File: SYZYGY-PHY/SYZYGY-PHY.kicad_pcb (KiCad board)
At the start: 4 copper layers, 57.7 x 27 mm, 48 parts, among them J1 QTH-020-01-X-D-DP-A, J2 ARJM11C7-502-KB-EW2, J3 Conn_01x10, U1 GPY111, U2 TXB0106RGY, U3 TXB0106RGY, Y1 Crystal_GND24

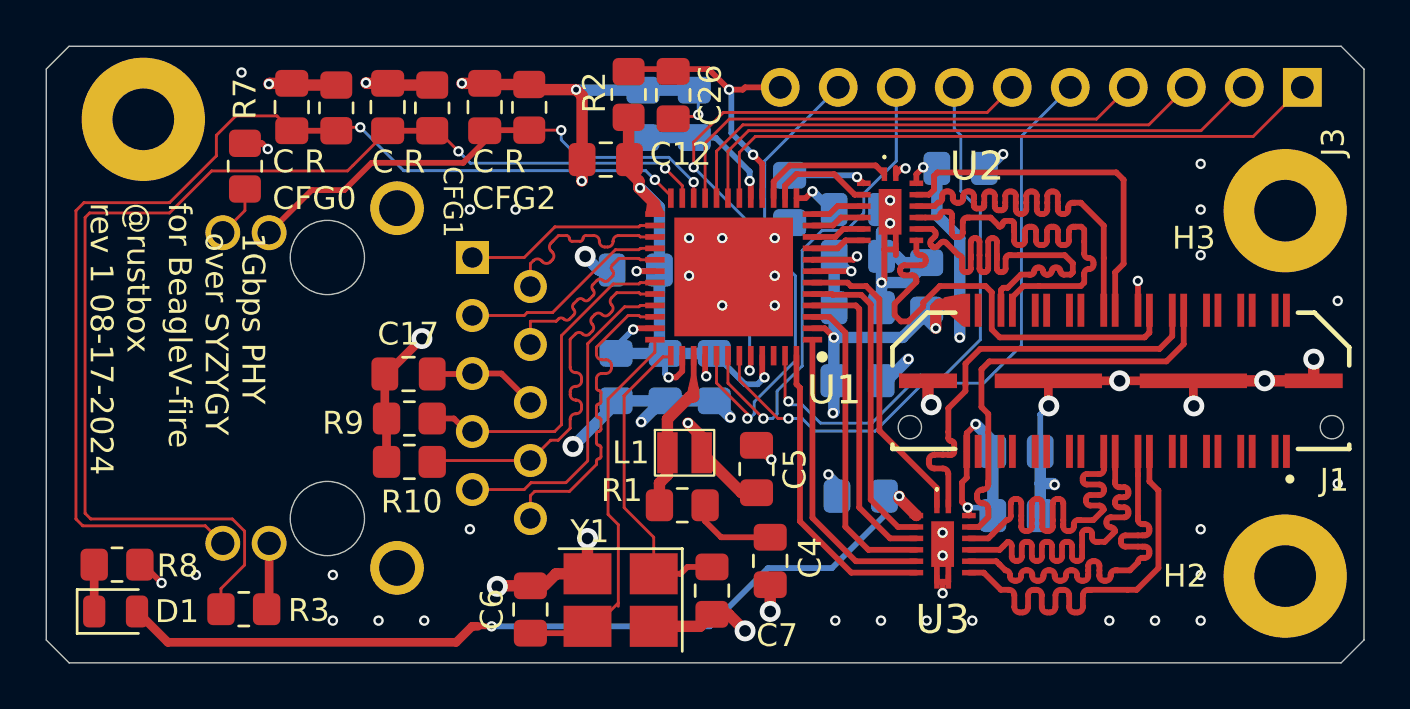
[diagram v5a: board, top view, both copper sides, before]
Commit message: adding a GND header, adding 3.3V and 1.8V 1x2 header
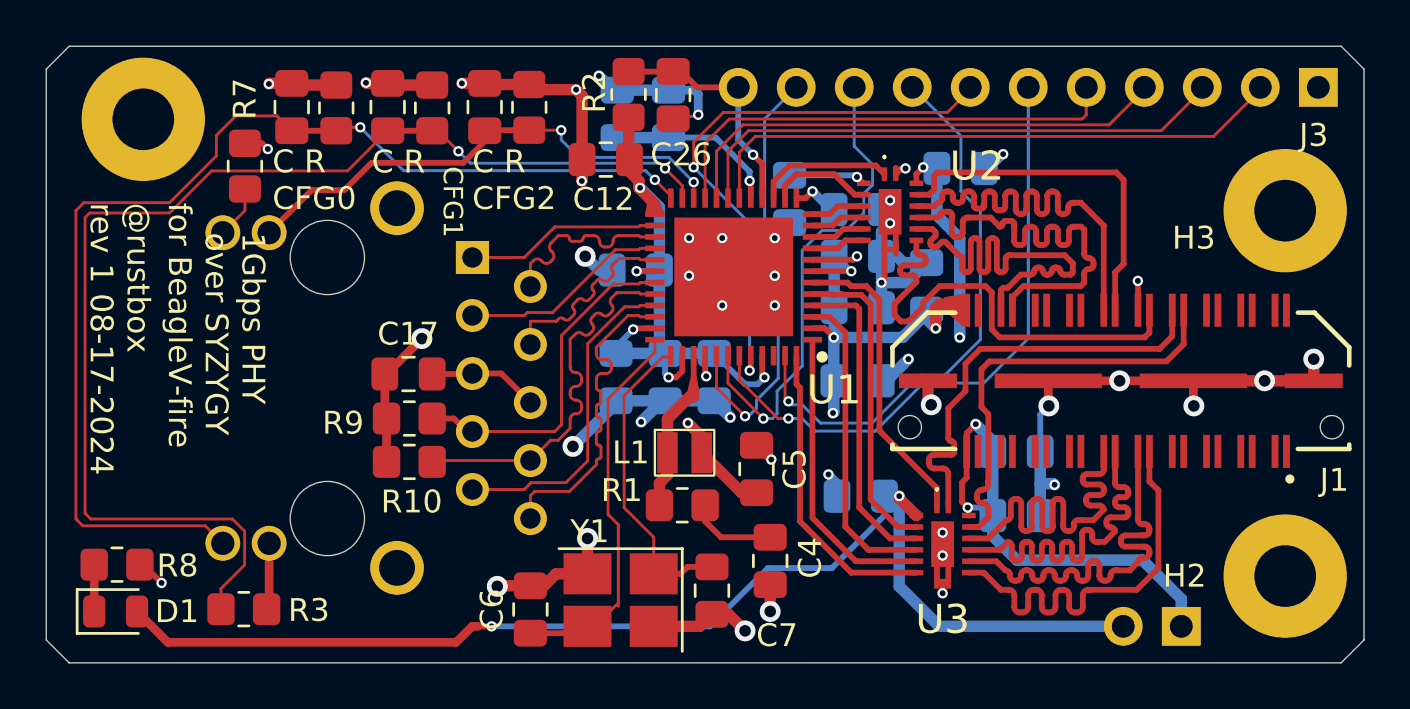
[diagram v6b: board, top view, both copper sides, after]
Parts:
- added J4: Conn_01x02, Connector_PinHeader_2.54mm:PinHeader_1x02_P2.54mm_Vertical, B.Cu at (139.7, 87.4)
- J3: value Conn_01x10 -> Conn_01x11; footprint Connector_PinSocket_2.54mm:PinSocket_1x10_P2.54mm_Vertical -> Connector_PinSocket_2.54mm:PinSocket_1x11_P2.54mm_Vertical
- moved C16 1.12 mm to (115.0, 65.0)
- moved C18 1.12 mm to (117.2, 65.0)
- moved J3 0.70 mm to (145.7, 63.8)
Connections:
- J3 pad 1: /TDI -> GND
- J3 pad 10: /RSTN -> /MDC
- J3 pad 2: /TCK -> /TDI
- J3 pad 3: /TMS -> /TCK
- J3 pad 4: /TDO -> /TMS
- J3 pad 5: /SCL -> /TDO
- J3 pad 6: /SDA -> /SCL
- J3 pad 7: /MDINT -> /SDA
- J3 pad 8: /MDIO -> /MDINT
- J3 pad 9: /MDC -> /MDIO
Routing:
- net +3V3: track 102.4 -> 116.2 mm
- net +1V8: track 23.3 -> 34.8 mm
- net GND: track 98.3 -> 107.6 mm, vias 64 -> 42
- net /RSTN: track 12.4 -> 10.4 mm, vias 2 -> 1
- net /MDC: track 20.6 -> 19.1 mm
- net /SDA: track 26.6 -> 25.2 mm
- net /TCK: track 25.8 -> 24.4 mm
- net /TMS: track 23.8 -> 22.3 mm
- net /TDI: track 27.8 -> 26.4 mm
- net /TDO: track 21.9 -> 20.8 mm
- net /VDDLC: track 35.1 -> 36.2 mm
- net /SCL: track 28.1 -> 27.3 mm
- net /MDINT: track 23.9 -> 24.7 mm
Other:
- board text added: "+1V8"
- board text added: "+3V3"
- board text added: "GND"

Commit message: make DRC happier with a "solid" connection
Instead of "thermal relief" where there isn't really room for it,
connect to the zones by just allowing the fill to pour over the whole
area.
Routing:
- net GND: track 107.6 -> 96.6 mm
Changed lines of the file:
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@@
 		(tags "mounting hole 2.7mm m2.5")
 		(property "Reference" "H1"
-			(at 3.85 -1.05 -0)
+			(at 3.85 -1.05 0)
 			(layer "B.SilkS")
 			(effects
@@
 		(tags "resistor handsolder")
 		(property "Reference" "R3"
-			(at 2.85 0.05 360)
+			(at 2.85 0.05 0)
 			(layer "F.SilkS")
 			(effects
@@
 		)
 		(property "Value" "RLED"
-			(at 0 1.65 360)
+			(at 0 1.65 0)
 			(layer "F.Fab")
 			(effects
@@
 		)
 		(fp_text user "${REFERENCE}"
-			(at 0 0 360)
+			(at 0 0 0)
 			(layer "F.Fab")
 			(effects
@@
 		)
 		(fp_text user "${REFERENCE}"
-			(at 0 -1.27 360)
+			(at 0 -1.27 0)
 			(layer "B.Fab")
 			(effects
@@
 		(tags "Through hole socket strip THT 1x11 2.54mm single row")
 		(property "Reference" "J3"
-			(at -2.1 -0.2 -180)
+			(at -2.1 -0.2 180)
 			(layer "F.SilkS")
 			(effects
@@
 		)
 		(fp_text user "${REFERENCE}"
-			(at 0 -12.7 360)
+			(at 0 -12.7 0)
 			(layer "B.Fab")
 			(effects
@@
 			(pinfunction "Pin_1")
 			(pintype "passive")
+			(zone_connect 2)
 		)
 		(pad "2" thru_hole oval
@@
 		(net 47)
 	)
-	(segment
-		(start 145.7 63.8)
-		(end 146.85 63.8)
-		(width 0.5)
-		(layer "In1.Cu")
-		(net 47)
-	)
-	(segment
-		(start 146.85 63.8)
-		(end 146.95 63.9)
-		(width 0.5)
-		(layer "In1.Cu")
-		(net 47)
-	)
-	(segment
-		(start 146.95 64)
-		(end 146.95 65.5)
-		(width 0.5)
-		(layer "In1.Cu")
-		(net 47)
-	)
-	(segment
-		(start 144.4 64.1)
-		(end 144.4 65.3)
-		(width 0.5)
-		(layer "In1.Cu")
-		(net 47)
-	)
-	(segment
-		(start 145.7 63.8)
-		(end 144.7 63.8)
-		(width 0.5)
-		(layer "In1.Cu")
-		(net 47)
-	)
-	(segment
-		(start 144.5 64)
-		(end 144.4 64.1)
-		(width 0.5)
-		(layer "In1.Cu")
-		(net 47)
-	)
-	(segment
-		(start 144.7 63.8)
-		(end 144.5 64)
-		(width 0.5)
-		(layer "In1.Cu")
-		(net 47)
-	)
-	(segment
-		(start 146.95 63.9)
-		(end 146.95 64)
-		(width 0.5)
-		(layer "In1.Cu")
-		(net 47)
-	)
-	(segment
-		(start 144.7 63.8)
-		(end 144.5 64)
-		(width 0.5)
-		(layer "In2.Cu")
-		(net 47)
-	)
-	(segment
-		(start 146.95 64)
-		(end 146.95 65.5)
-		(width 0.5)
-		(layer "In2.Cu")
-		(net 47)
-	)
-	(segment
-		(start 145.7 63.8)
-		(end 146.85 63.8)
-		(width 0.5)
-		(layer "In2.Cu")
-		(net 47)
-	)
-	(segment
-		(start 144.5 64)
-		(end 144.4 64.1)
-		(width 0.5)
-		(layer "In2.Cu")
-		(net 47)
-	)
-	(segment
-		(start 146.85 63.8)
-		(end 146.95 63.9)
-		(width 0.5)
-		(layer "In2.Cu")
-		(net 47)
-	)
-	(segment
-		(start 144.4 64.1)
-		(end 144.4 65.3)
-		(width 0.5)
-		(layer "In2.Cu")
-		(net 47)
-	)
-	(segment
-		(start 146.95 63.9)
-		(end 146.95 64)
-		(width 0.5)
-		(layer "In2.Cu")
-		(net 47)
-	)
-	(segment
-		(start 145.7 63.8)
-		(end 144.7 63.8)
-		(width 0.5)
-		(layer "In2.Cu")
-		(net 47)
-	)

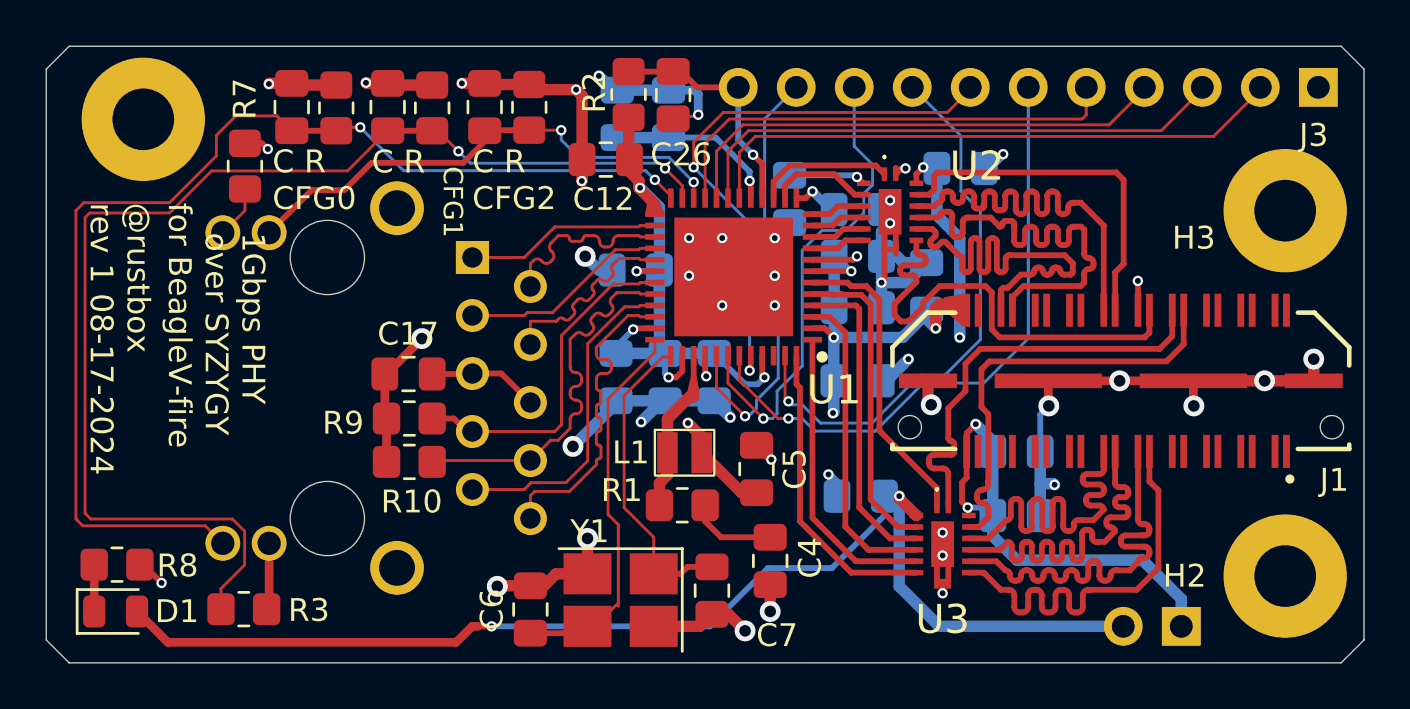
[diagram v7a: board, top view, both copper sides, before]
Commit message: adding SYZYGY breakout board, ready for review
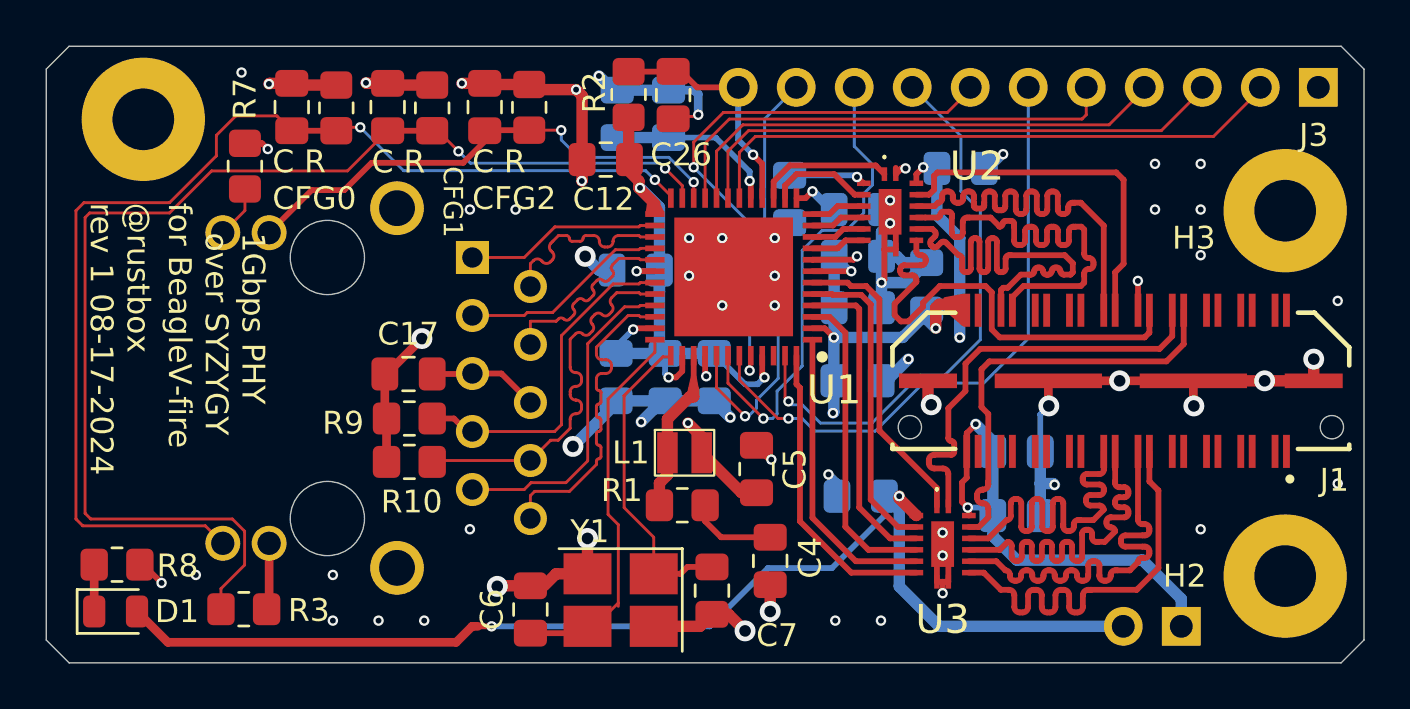
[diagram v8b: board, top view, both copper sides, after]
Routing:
- net GND: vias 42 -> 61
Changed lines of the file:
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@@
 	)
 	(via
+		(at 110.55 69.15)
+		(size 0.4572)
+		(drill 0.254)
+		(layers "F.Cu" "B.Cu")
+		(free yes)
+		(net 47)
+	)
+	(via
+		(at 140.55 71.15)
+		(size 0.4572)
+		(drill 0.254)
+		(layers "F.Cu" "B.Cu")
+		(free yes)
+		(net 47)
+	)
+	(via
 		(at 121.9 73.35)
 		(size 0.4572)
@@
 	)
 	(via
+		(at 126.55 87.15)
+		(size 0.4572)
+		(drill 0.254)
+		(layers "F.Cu" "B.Cu")
+		(free yes)
+		(net 47)
+	)
+	(via
 		(at 134.15 81.2)
 		(size 0.4572)
@@
 	)
 	(via
+		(at 146.55 73.15)
+		(size 0.4572)
+		(drill 0.254)
+		(layers "F.Cu" "B.Cu")
+		(free yes)
+		(net 47)
+	)
+	(via
+		(at 140.55 67.15)
+		(size 0.4572)
+		(drill 0.254)
+		(layers "F.Cu" "B.Cu")
+		(free yes)
+		(net 47)
+	)
+	(via
+		(at 98.55 63.15)
+		(size 0.4572)
+		(drill 0.254)
+		(layers "F.Cu" "B.Cu")
+		(free yes)
+		(net 47)
+	)
+	(via
+		(at 106.55 87.15)
+		(size 0.4572)
+		(drill 0.254)
+		(layers "F.Cu" "B.Cu")
+		(free yes)
+		(net 47)
+	)
+	(via
+		(at 146.55 81.15)
+		(size 0.4572)
+		(drill 0.254)
+		(layers "F.Cu" "B.Cu")
+		(free yes)
+		(net 47)
+	)
+	(via
 		(at 119.6 70.4)
 		(size 0.4572)
@@
 	)
 	(via
+		(at 96.55 85.15)
+		(size 0.4572)
+		(drill 0.254)
+		(layers "F.Cu" "B.Cu")
+		(free yes)
+		(net 47)
+	)
+	(via
+		(at 108.55 83.15)
+		(size 0.4572)
+		(drill 0.254)
+		(layers "F.Cu" "B.Cu")
+		(free yes)
+		(net 47)
+	)
+	(via
+		(at 102.55 85.15)
+		(size 0.4572)
+		(drill 0.254)
+		(layers "F.Cu" "B.Cu")
+		(free yes)
+		(net 47)
+	)
+	(via
+		(at 108.55 69.15)
+		(size 0.4572)
+		(drill 0.254)
+		(layers "F.Cu" "B.Cu")
+		(free yes)
+		(net 47)
+	)
+	(via
+		(at 140.55 83.15)
+		(size 0.4572)
+		(drill 0.254)
+		(layers "F.Cu" "B.Cu")
+		(free yes)
+		(net 47)
+	)
+	(via
 		(at 126.95 68.75)
 		(size 0.4572)
@@
 	)
 	(via
+		(at 102.55 87.15)
+		(size 0.4572)
+		(drill 0.254)
+		(layers "F.Cu" "B.Cu")
+		(free yes)
+		(net 47)
+	)
+	(via
 		(at 120.6 87.6)
 		(size 0.9144)
@@
 	)
 	(via
+		(at 124.55 87.15)
+		(size 0.4572)
+		(drill 0.254)
+		(layers "F.Cu" "B.Cu")
+		(free yes)
+		(net 47)
+	)
+	(via
 		(at 121.7 86.75)
 		(size 0.9144)
@@
 	)
 	(via
+		(at 140.55 69.15)
+		(size 0.4572)
+		(drill 0.254)
+		(layers "F.Cu" "B.Cu")
+		(free yes)
+		(net 47)
+	)
+	(via
+		(at 138.55 69.15)
+		(size 0.4572)
+		(drill 0.254)
+		(layers "F.Cu" "B.Cu")
+		(free yes)
+		(net 47)
+	)
+	(via
 		(at 143.35 76.65)
 		(size 0.9144)
@@
 	)
 	(via
+		(at 138.55 67.15)
+		(size 0.4572)
+		(drill 0.254)
+		(layers "F.Cu" "B.Cu")
+		(free yes)
+		(net 47)
+	)
+	(via
 		(at 129.25 85.95)
 		(size 0.4572)
@@
 	)
 	(via
+		(at 104.55 87.15)
+		(size 0.4572)
+		(drill 0.254)
+		(layers "F.Cu" "B.Cu")
+		(free yes)
+		(net 47)
+	)
+	(via
 		(at 119.6 73.35)
 		(size 0.4572)
@@
 		)
 	)
+	(group "ViaStitching GND"
+		(members "012bf0e7-e1c8-4f8b-afde-765f695f1f94" "050bb13d-ff57-459c-92ac-8af64a13e5b7"
+			"15e84928-b4b9-49cf-8ec4-e37d092e657c" "24c13111-2b68-46b2-bb42-6b4d42d6c8b3"
+			"288cc818-6c7f-40cf-b4c8-7038251a42bc" "28bb4c15-b43f-48c3-885a-fe35c36f686c"
+			"31be3fc6-9df5-404c-96c5-4fd9a81ece1c" "3bddb0a7-4f00-4945-9ddf-eeeb87114dbb"
+			"49ea42c7-e93a-4924-897e-45c7de2490fc" "4b11e3b1-93e3-46ff-834f-9c93faa4f53d"
+			"4bef9c22-1594-411d-97e2-0953e50513ef" "507522a4-5d7f-4347-8476-f37858a2874a"
+			"5567c03b-3b77-48d1-8fc6-a11ca0229f6c" "6f3165d0-c7be-4740-b59c-1d5905d2c820"
+			"824d066e-24cd-4a08-ae04-b3efc8fdaaf0" "c972709a-db2f-4bea-ae6b-14ae87e46e88"
+			"cb135b77-31bb-4bba-acbb-357321cae33b" "e4ae259d-87e8-465d-835d-8851f205f941"
+			"ec1c0d64-e864-4b3d-8ea3-eac04602cccb"
+		)
+	)
